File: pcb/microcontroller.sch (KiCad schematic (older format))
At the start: 22 parts, among them J3 Conn_02x03_Odd_Even, J4 Conn_01x04, J5 USB_B, SW1 SW_Push, U1 ATXMEGA192C3-AU, U3 USBLC6-2SC6

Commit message: Version 2 PCB design (WIP)
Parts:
- C9: renamed from C11; footprint Capacitors_SMD:C_0805_HandSoldering -> Capacitors_SMD:C_1206_HandSoldering
- J3: renamed from J5; footprint Connectors:USB_B -> Local:Multicomp_MC32597
- renumbered C3 to C1, C4 to C2, C5 to C3, C6 to C4, C7 to C5, C8 to C6, C10 to C8, J3 to J7, J4 to J8, R31 to R1, R32 to R2, R33 to R3, R34 to R4, TP36 to TP1, TP37 to TP2, TP38 to TP3, TP39 to TP4
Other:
- note added: "R1 and C8 form an EMI filter\nas recommended by Atmel\napplication note AVR1017."
- note removed: "R31 and C10 form an EMI filter\nas recommended by Atmel\napplication note AVR1017."
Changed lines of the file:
@@
 LIBS:valves
 LIBS:symbols
-LIBS:tape-punch-controller-cache
 EELAYER 25 0
 EELAYER END
@@
 	4200 4450 5150 4450
 $Comp
-L C C3
+L C C1
 U 1 1 5A3BD480
 P 8200 1900
-F 0 "C3" H 8225 2000 50  0000 L CNN
+F 0 "C1" H 8225 2000 50  0000 L CNN
 F 1 "100n" H 8225 1800 50  0000 L CNN
 F 2 "Capacitors_SMD:C_0805_HandSoldering" H 8238 1750 50  0001 C CNN
@@
 $EndComp
 $Comp
-L C C4
+L C C2
 U 1 1 5A3BD62D
 P 8600 1900
-F 0 "C4" H 8625 2000 50  0000 L CNN
+F 0 "C2" H 8625 2000 50  0000 L CNN
 F 1 "100n" H 8625 1800 50  0000 L CNN
 F 2 "Capacitors_SMD:C_0805_HandSoldering" H 8638 1750 50  0001 C CNN
@@
 $EndComp
 $Comp
-L C C5
+L C C3
 U 1 1 5A3BD7E3
 P 9000 1900
-F 0 "C5" H 9025 2000 50  0000 L CNN
+F 0 "C3" H 9025 2000 50  0000 L CNN
 F 1 "100n" H 9025 1800 50  0000 L CNN
 F 2 "Capacitors_SMD:C_0805_HandSoldering" H 9038 1750 50  0001 C CNN
@@
 $EndComp
 $Comp
-L C C6
+L C C4
 U 1 1 5A3BD7E9
 P 9400 1900
-F 0 "C6" H 9425 2000 50  0000 L CNN
+F 0 "C4" H 9425 2000 50  0000 L CNN
 F 1 "100n" H 9425 1800 50  0000 L CNN
 F 2 "Capacitors_SMD:C_0805_HandSoldering" H 9438 1750 50  0001 C CNN
@@
 $EndComp
 $Comp
-L C C7
+L C C5
 U 1 1 5A3BD8F0
 P 9800 1900
-F 0 "C7" H 9825 2000 50  0000 L CNN
+F 0 "C5" H 9825 2000 50  0000 L CNN
 F 1 "100n" H 9825 1800 50  0000 L CNN
 F 2 "Capacitors_SMD:C_0805_HandSoldering" H 9838 1750 50  0001 C CNN
@@
 $EndComp
 $Comp
-L C C8
+L C C6
 U 1 1 5A3BD8F6
 P 10200 1900
-F 0 "C8" H 10225 2000 50  0000 L CNN
+F 0 "C6" H 10225 2000 50  0000 L CNN
 F 1 "100n" H 10225 1800 50  0000 L CNN
 F 2 "Capacitors_SMD:C_0805_HandSoldering" H 10238 1750 50  0001 C CNN
@@
 	5000 2150 5150 2150
 $Comp
-L Conn_01x04 J4
+L Conn_01x04 J8
 U 1 1 5A3CD68A
 P 2400 3650
-F 0 "J4" H 2400 3850 50  0000 C CNN
+F 0 "J8" H 2400 3850 50  0000 C CNN
 F 1 "Conn_01x04" H 2400 3350 50  0000 C CNN
 F 2 "Pin_Headers:Pin_Header_Straight_1x04_Pitch2.54mm" H 2400 3650 50  0001 C CNN
@@
 	2000 3850 2200 3850
 $Comp
-L Conn_02x03_Odd_Even J3
+L Conn_02x03_Odd_Even J7
 U 1 1 5A3CE0A6
 P 2400 1750
-F 0 "J3" H 2450 1950 50  0000 C CNN
+F 0 "J7" H 2450 1950 50  0000 C CNN
 F 1 "Conn_02x03_Odd_Even" H 2450 1550 50  0000 C CNN
 F 2 "Pin_Headers:Pin_Header_Straight_2x03_Pitch2.54mm" H 2400 1750 50  0001 C CNN
@@
 PDI (program/debug interface) connector.\nPinout is same as suggested in Atmel\napplication note AT016017.
 $Comp
-L USB_B J5
+L USB_B J3
 U 1 1 5A3D0F19
 P 1550 5900
-F 0 "J5" H 1350 6350 50  0000 L CNN
+F 0 "J3" H 1350 6350 50  0000 L CNN
 F 1 "USB_B" H 1350 6250 50  0000 L CNN
-F 2 "Connectors:USB_B" H 1700 5850 50  0001 C CNN
+F 2 "Local:Multicomp_MC32597" H 1700 5850 50  0001 C CNN
 F 3 "" H 1700 5850 50  0001 C CNN
 	1    1550 5900
@@
 	3100 6050 3200 6050
 $Comp
-L R R31
+L R R1
 U 1 1 5A3D57D2
 P 1600 6700
-F 0 "R31" V 1680 6700 50  0000 C CNN
+F 0 "R1" V 1680 6700 50  0000 C CNN
 F 1 "1M" V 1600 6700 50  0000 C CNN
 F 2 "Resistors_SMD:R_0805_HandSoldering" V 1530 6700 50  0001 C CNN
@@
 $EndComp
 $Comp
-L C C10
+L C C8
 U 1 1 5A3D5947
 P 1300 6700
-F 0 "C10" H 1325 6800 50  0000 L CNN
+F 0 "C8" H 1325 6800 50  0000 L CNN
 F 1 "4.7n" H 1325 6600 50  0000 L CNN
 F 2 "Capacitors_SMD:C_0805_HandSoldering" H 1338 6550 50  0001 C CNN
@@
 Connection ~ 1450 6900
 $Comp
-L R R32
+L R R2
 U 1 1 5A3D6831
 P 3850 5800
-F 0 "R32" V 3930 5800 50  0000 C CNN
+F 0 "R2" V 3930 5800 50  0000 C CNN
 F 1 "1k" V 3850 5800 50  0000 C CNN
 F 2 "Resistors_SMD:R_0805_HandSoldering" V 3780 5800 50  0001 C CNN
@@
 $EndComp
 $Comp
-L R R33
+L R R3
 U 1 1 5A3D696C
 P 3850 6200
-F 0 "R33" V 3930 6200 50  0000 C CNN
+F 0 "R3" V 3930 6200 50  0000 C CNN
 F 1 "1k" V 3850 6200 50  0000 C CNN
 F 2 "Resistors_SMD:R_0805_HandSoldering" V 3780 6200 50  0001 C CNN
@@
 USB connector.
 $Comp
-L C C11
+L C C9
 U 1 1 5A3D905C
 P 4250 6200
-F 0 "C11" H 4275 6300 50  0000 L CNN
+F 0 "C9" H 4275 6300 50  0000 L CNN
 F 1 "10u" H 4275 6100 50  0000 L CNN
-F 2 "Capacitors_SMD:C_0805_HandSoldering" H 4288 6050 50  0001 C CNN
+F 2 "Capacitors_SMD:C_1206_HandSoldering" H 4288 6050 50  0001 C CNN
 F 3 "" H 4250 6200 50  0001 C CNN
 	1    4250 6200
@@
 USB_SENSE is high when a\nUSB cable is plugged in. The\ncapacitor forms a debouncing\nfilter with the resistors in the\nvoltage divider.
 Text Notes 850  7500 0    60   ~ 0
-R31 and C10 form an EMI filter\nas recommended by Atmel\napplication note AVR1017.
-$Comp
-L R R34
+R1 and C8 form an EMI filter\nas recommended by Atmel\napplication note AVR1017.
+$Comp
+L R R4
 U 1 1 5A3DAF44
 P 9400 3950
-F 0 "R34" V 9480 3950 50  0000 C CNN
+F 0 "R4" V 9480 3950 50  0000 C CNN
 F 1 "10k" V 9400 3950 50  0000 C CNN
 F 2 "Resistors_SMD:R_0805_HandSoldering" V 9330 3950 50  0001 C CNN
@@
 USB_SHIELD
 $Comp
-L TEST TP37
+L TEST TP2
 U 1 1 5A43F555
 P 1900 1900
-F 0 "TP37" H 1900 2200 50  0000 C BNN
+F 0 "TP2" H 1900 2200 50  0000 C BNN
 F 1 "TEST" H 1900 2150 50  0000 C CNN
 F 2 "Measurement_Points:Measurement_Point_Round-SMD-Pad_Small" H 1900 1900 50  0001 C CNN
@@
 $EndComp
 $Comp
-L TEST TP36
+L TEST TP1
 U 1 1 5A43F61C
 P 1900 1600
-F 0 "TP36" H 1900 1900 50  0000 C BNN
+F 0 "TP1" H 1900 1900 50  0000 C BNN
 F 1 "TEST" H 1900 1850 50  0000 C CNN
 F 2 "Measurement_Points:Measurement_Point_Round-SMD-Pad_Small" H 1900 1600 50  0001 C CNN
@@
 Connection ~ 1900 1650
 $Comp
-L TEST TP39
+L TEST TP4
 U 1 1 5A4492E4
 P 4250 5950
-F 0 "TP39" H 4250 6250 50  0000 C BNN
+F 0 "TP4" H 4250 6250 50  0000 C BNN
 F 1 "TEST" H 4250 6200 50  0000 C CNN
 F 2 "Measurement_Points:Measurement_Point_Round-SMD-Pad_Small" H 4250 5950 50  0001 C CNN
@@
 $EndComp
 $Comp
-L TEST TP38
+L TEST TP3
 U 1 1 5A4493A9
 P 3850 5500
-F 0 "TP38" H 3850 5800 50  0000 C BNN
+F 0 "TP3" H 3850 5800 50  0000 C BNN
 F 1 "TEST" H 3850 5750 50  0000 C CNN
 F 2 "Measurement_Points:Measurement_Point_Round-SMD-Pad_Small" H 3850 5500 50  0001 C CNN

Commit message: Finish draft of second version of PCB
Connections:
- net CANCEL_n: now also U1.63 (AC1/ADC1/PA1); no longer U1.37 (PE1/OC0B/XCK0/SCL)
- net CONFIRM_n: now also U1.64 (AC2/ADC2/PA2); no longer U1.36 (PE0/OC0A/SDA)
- net FEED_SIG: now also U1.62 (AREFA/AC0/ADC0/PA0); no longer U1.43 (PE7/TOSC1/CLKP/EVOUT)
- net GND: now also U1.21 (MOSI/OC0CHS/OC1B/PC5), U1.22 (RTCOUT/MISO/~OC0DLS~/PC6), U1.23 (EVOUT/CLKP/SCK/OC0DHS/PC7), U1.36 (PE0/OC0A/SDA), U1.37 (PE1/OC0B/XCK0/SCL), U1.38 (PE2/OC0C/RXD0), U1.43 (PE7/TOSC1/CLKP/EVOUT); no longer U1.1 (AC3/ADC3/PA3), U1.12 (ADC14/PB6), U1.13 (ADC15/PB7), U1.2 (AC4/ADC4/PA4), U1.62 (AREFA/AC0/ADC0/PA0), U1.63 (AC1/ADC1/PA1), U1.64 (AC2/ADC2/PA2)
- net LCD_E: now also U1.13 (ADC15/PB7); no longer U1.20 (~SS~/~OC0CLS~/OC1A/PC4)
- net LCD_RS: now also U1.12 (ADC14/PB6); no longer U1.21 (MOSI/OC0CHS/OC1B/PC5)
- net LOW_TAPE: now also U1.41 (PE5); no longer U1.40 (PE4)
- net NO_TAPE: now also U1.40 (PE4); no longer U1.41 (PE5)
- net STAT_GRN: now also U1.1 (AC3/ADC3/PA3); no longer U1.22 (RTCOUT/MISO/~OC0DLS~/PC6)
- net STAT_RED: now also U1.2 (AC4/ADC4/PA4); no longer U1.23 (EVOUT/CLKP/SCK/OC0DHS/PC7)
- net SYNC: now also U1.39 (PE3/OC0D/TXD0); no longer U1.38 (PE2/OC0C/RXD0)
- net USB_SENSE: now also U1.20 (~SS~/~OC0CLS~/OC1A/PC4); no longer U1.39 (PE3/OC0D/TXD0)
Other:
- moved on the sheet: C1, C2, C3, C4, C5, C6

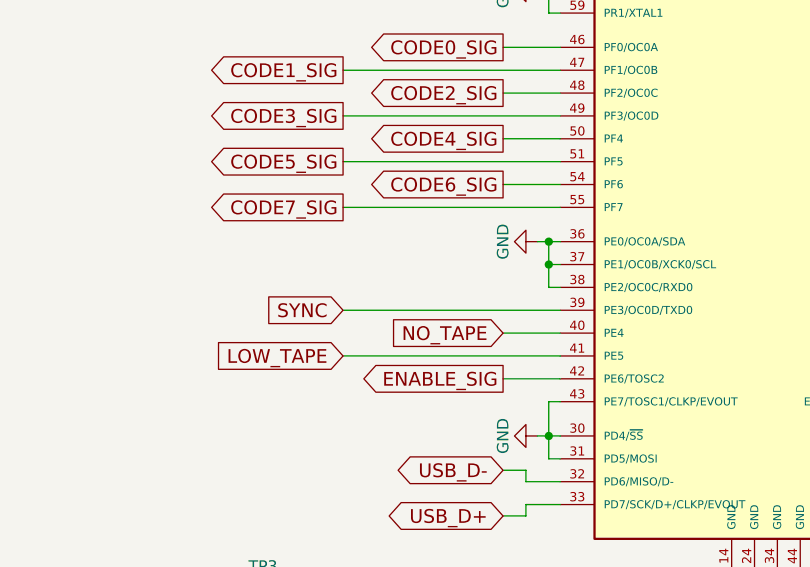
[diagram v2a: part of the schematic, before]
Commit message: pcb: fix SYNC being wired to wrong pin (should be PE2, not PE3)
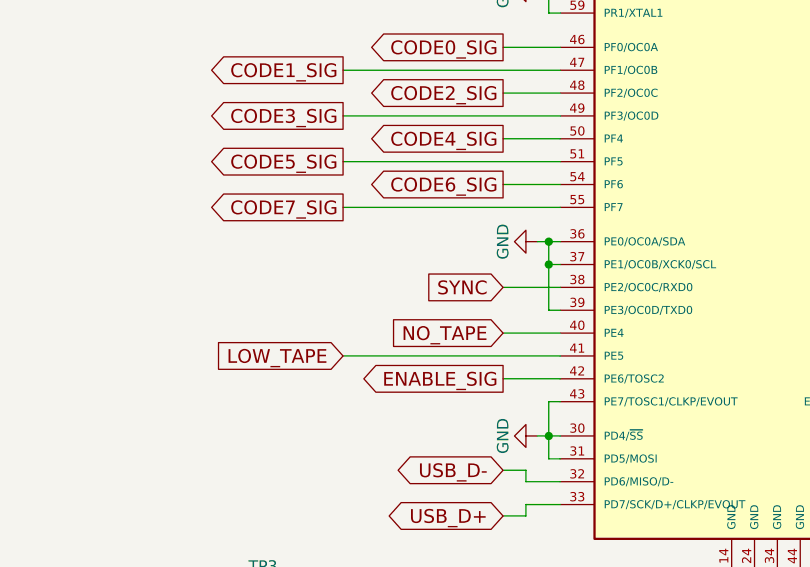
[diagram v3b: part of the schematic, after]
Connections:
- net GND: now also U1.39 (PE3/OC0D/TXD0); no longer U1.38 (PE2/OC0C/RXD0)
- net SYNC: now also U1.38 (PE2/OC0C/RXD0); no longer U1.39 (PE3/OC0D/TXD0)
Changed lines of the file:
@@
 Text GLabel 7400 4150 2    60   Input ~ 0
 USB_SENSE
-Text GLabel 4200 4050 0    60   Input ~ 0
+Text GLabel 4900 3950 0    60   Input ~ 0
 SYNC
 Text GLabel 7400 2150 2    60   Input ~ 0
@@
 	5050 3750 5150 3750
 Wire Wire Line
-	5100 3750 5100 3950
-Wire Wire Line
 	5100 3850 5150 3850
 Connection ~ 5100 3750
@@
 	7400 4150 7150 4150
 Wire Wire Line
-	5100 3950 5150 3950
+	5100 3750 5100 4050
+Wire Wire Line
+	5100 4050 5150 4050
 Connection ~ 5100 3850
 Wire Wire Line
-	5150 4050 4200 4050
+	4900 3950 5150 3950
 $EndSCHEMATC

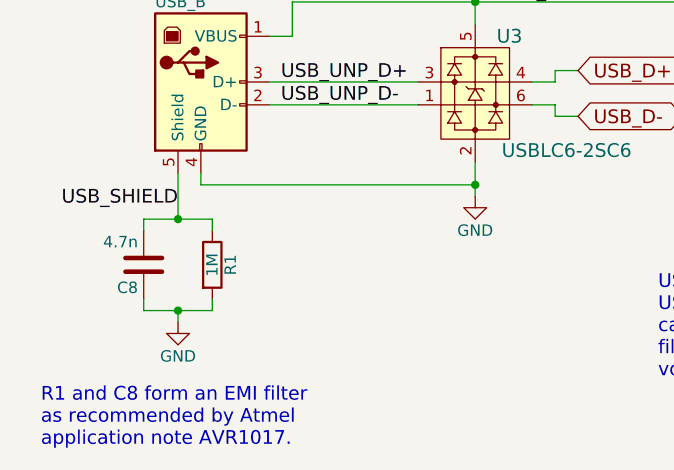
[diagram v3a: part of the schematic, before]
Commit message: pcb: connect negative side of USB ESD protection IC to USB_SHIELD rather than GND, as per document AVR1017
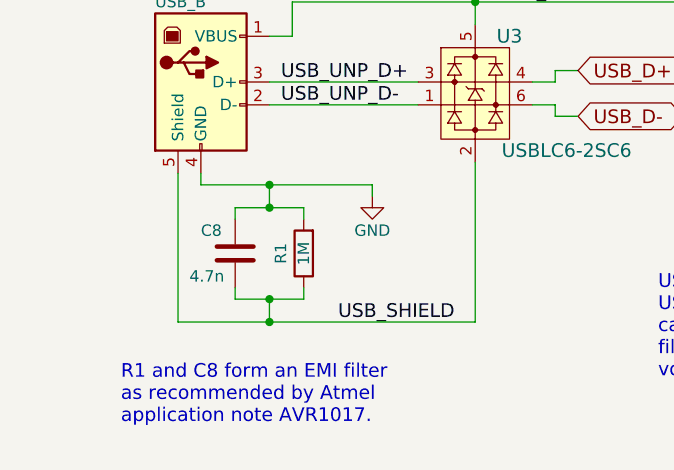
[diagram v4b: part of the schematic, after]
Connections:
- net GND: no longer U3.2 (GND)
- net USB_SHIELD: now also U3.2 (GND)
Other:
- moved on the sheet: C8, R1
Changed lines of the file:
@@
 L R R1
 U 1 1 5A3D57D2
-P 1600 6700
-F 0 "R1" V 1680 6700 50  0000 C CNN
-F 1 "1M" V 1600 6700 50  0000 C CNN
-F 2 "Resistors_SMD:R_0805_HandSoldering" V 1530 6700 50  0001 C CNN
-F 3 "" H 1600 6700 50  0001 C CNN
-	1    1600 6700
-	1    0    0    -1
+P 2000 6650
+F 0 "R1" V 2100 6650 50  0000 C CNN
+F 1 "1M" V 2000 6650 50  0000 C CNN
+F 2 "Resistors_SMD:R_0805_HandSoldering" V 1930 6650 50  0001 C CNN
+F 3 "" H 2000 6650 50  0001 C CNN
+	1    2000 6650
+	-1   0    0    1
 $EndComp
 $Comp
 L C C8
 U 1 1 5A3D5947
-P 1300 6700
-F 0 "C8" H 1325 6800 50  0000 L CNN
-F 1 "4.7n" H 1325 6600 50  0000 L CNN
-F 2 "Capacitors_SMD:C_0805_HandSoldering" H 1338 6550 50  0001 C CNN
-F 3 "" H 1300 6700 50  0001 C CNN
-	1    1300 6700
-	-1   0    0    1
+P 1700 6650
+F 0 "C8" H 1550 6750 50  0000 L CNN
+F 1 "4.7n" H 1500 6550 50  0000 L CNN
+F 2 "Capacitors_SMD:C_0805_HandSoldering" H 1738 6500 50  0001 C CNN
+F 3 "" H 1700 6650 50  0001 C CNN
+	1    1700 6650
+	1    0    0    -1
 $EndComp
 $Comp
 L GND #PWR013
 U 1 1 5A3D647F
-P 1450 6950
-F 0 "#PWR013" H 1450 6700 50  0001 C CNN
-F 1 "GND" H 1450 6800 50  0000 C CNN
-F 2 "" H 1450 6950 50  0001 C CNN
-F 3 "" H 1450 6950 50  0001 C CNN
-	1    1450 6950
+P 2300 6400
+F 0 "#PWR013" H 2300 6150 50  0001 C CNN
+F 1 "GND" H 2300 6250 50  0000 C CNN
+F 2 "" H 2300 6400 50  0001 C CNN
+F 3 "" H 2300 6400 50  0001 C CNN
+	1    2300 6400
 	1    0    0    -1
 $EndComp
@@
 Text Label 2850 5550 0    60   ~ 0
 USB_VBUS
-$Comp
-L GND #PWR015
-U 1 1 5A3D726C
-P 2750 6400
-F 0 "#PWR015" H 2750 6150 50  0001 C CNN
-F 1 "GND" H 2750 6250 50  0000 C CNN
-F 2 "" H 2750 6400 50  0001 C CNN
-F 3 "" H 2750 6400 50  0001 C CNN
-	1    2750 6400
-	1    0    0    -1
-$EndComp
 Text GLabel 4450 6000 2    60   Output ~ 0
 USB_SENSE
@@
 Text Notes 3550 7200 0    60   ~ 0
 USB_SENSE is high when a\nUSB cable is plugged in. The\ncapacitor forms a debouncing\nfilter with the resistors in the\nvoltage divider.
-Text Notes 850  7500 0    60   ~ 0
+Text Notes 1200 7400 0    60   ~ 0
 R1 and C8 form an EMI filter\nas recommended by Atmel\napplication note AVR1017.
 $Comp
@@
 $EndComp
 $Comp
-L GND #PWR016
+L GND #PWR015
 U 1 1 5A3DB353
 P 9400 4650
-F 0 "#PWR016" H 9400 4400 50  0001 C CNN
+F 0 "#PWR015" H 9400 4400 50  0001 C CNN
 F 1 "GND" H 9400 4500 50  0000 C CNN
 F 2 "" H 9400 4650 50  0001 C CNN
@@
 $EndComp
 $Comp
-L +3.3V #PWR017
+L +3.3V #PWR016
 U 1 1 5A3DB39D
 P 9400 3750
-F 0 "#PWR017" H 9400 3600 50  0001 C CNN
+F 0 "#PWR016" H 9400 3600 50  0001 C CNN
 F 1 "+3.3V" H 9400 3890 50  0000 C CNN
 F 2 "" H 9400 3750 50  0001 C CNN
@@
 Text Notes 9550 3450 0    60   ~ 0
 Reset button.
-Text Label 1450 6450 2    60   ~ 0
-USB_SHIELD
 $Comp
 L TEST TP2
@@
 USB_UNP_D-
 $Comp
-L GND #PWR018
+L GND #PWR017
 U 1 1 5A3BE5D1
 P 7250 2550
-F 0 "#PWR018" H 7250 2300 50  0001 C CNN
+F 0 "#PWR017" H 7250 2300 50  0001 C CNN
 F 1 "GND" H 7250 2400 50  0000 C CNN
 F 2 "" H 7250 2550 50  0001 C CNN
@@
 $EndComp
 $Comp
-L GND #PWR019
+L GND #PWR018
 U 1 1 5A5D1B87
 P 5050 3750
-F 0 "#PWR019" H 5050 3500 50  0001 C CNN
+F 0 "#PWR018" H 5050 3500 50  0001 C CNN
 F 1 "GND" H 5050 3600 50  0000 C CNN
 F 2 "" H 5050 3750 50  0001 C CNN
@@
 	2750 5550 2750 5650
 Wire Wire Line
-	1550 6300 1550 6350
-Wire Wire Line
-	2750 6250 2750 6400
-Wire Wire Line
 	3000 5900 3100 5900
 Wire Wire Line
@@
 	3100 6050 3200 6050
 Wire Wire Line
-	1300 6550 1300 6500
-Wire Wire Line
-	1300 6500 1600 6500
-Wire Wire Line
-	1600 6500 1600 6550
-Wire Wire Line
-	1300 6850 1300 6900
-Wire Wire Line
-	1300 6900 1600 6900
-Wire Wire Line
-	1600 6900 1600 6850
-Wire Wire Line
-	1450 6300 1450 6500
-Connection ~ 1450 6500
-Wire Wire Line
-	1450 6950 1450 6900
-Connection ~ 1450 6900
+	1700 6500 1700 6450
+Wire Wire Line
+	1700 6450 2000 6450
+Wire Wire Line
+	2000 6450 2000 6500
+Wire Wire Line
+	1700 6800 1700 6850
+Wire Wire Line
+	1700 6850 2000 6850
+Wire Wire Line
+	2000 6850 2000 6800
 Wire Wire Line
 	3850 5950 3850 6050
@@
 	3850 5500 3850 5650
 Connection ~ 2750 5550
-Connection ~ 2750 6350
 Wire Wire Line
 	3850 6000 4450 6000
@@
 	1850 6000 2500 6000
 Wire Wire Line
-	1550 6350 2750 6350
-Wire Wire Line
 	8100 2050 7150 2050
 Wire Wire Line
@@
 Wire Wire Line
 	4900 3950 5150 3950
+Wire Wire Line
+	1550 6350 2300 6350
+Wire Wire Line
+	2300 6350 2300 6400
+Wire Wire Line
+	1850 6450 1850 6350
+Connection ~ 1850 6450
+Wire Wire Line
+	1550 6350 1550 6300
+Connection ~ 1850 6350
+Wire Wire Line
+	1450 6300 1450 6950
+Wire Wire Line
+	1450 6950 2750 6950
+Wire Wire Line
+	1850 6950 1850 6850
+Connection ~ 1850 6850
+Wire Wire Line
+	2750 6950 2750 6250
+Connection ~ 1850 6950
+Text Label 2150 6950 0    60   ~ 0
+USB_SHIELD
 $EndSCHEMATC
